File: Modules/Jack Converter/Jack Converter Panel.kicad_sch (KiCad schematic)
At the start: 39 parts

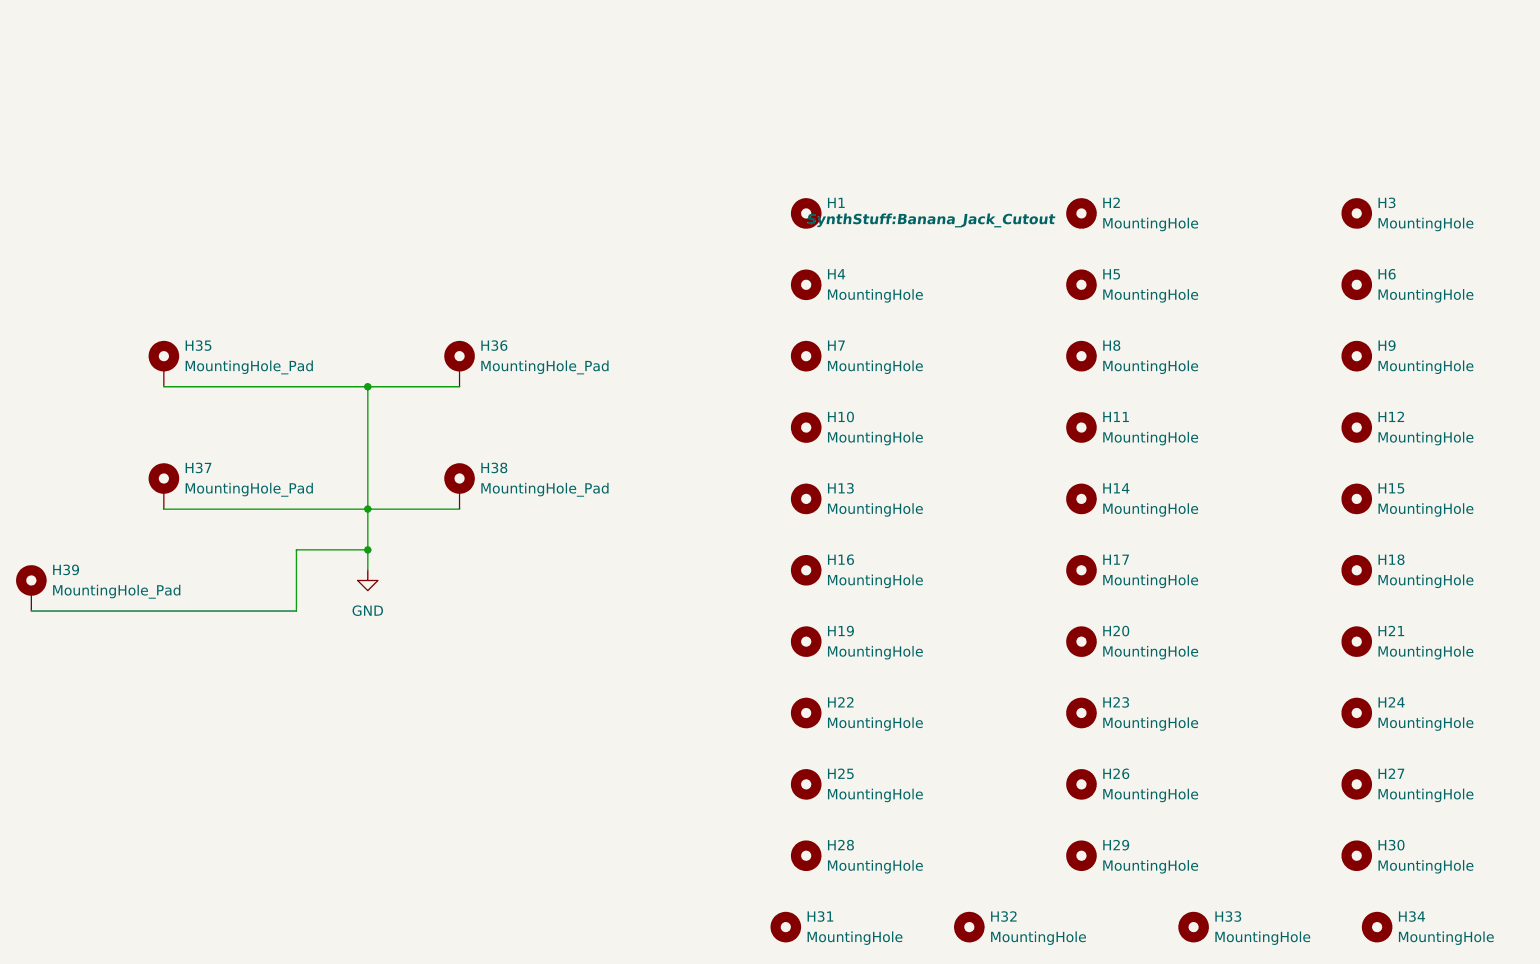
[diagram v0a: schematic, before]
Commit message: Front panel design ongoing
Deleted spacer hole, positioned all holes, started decals
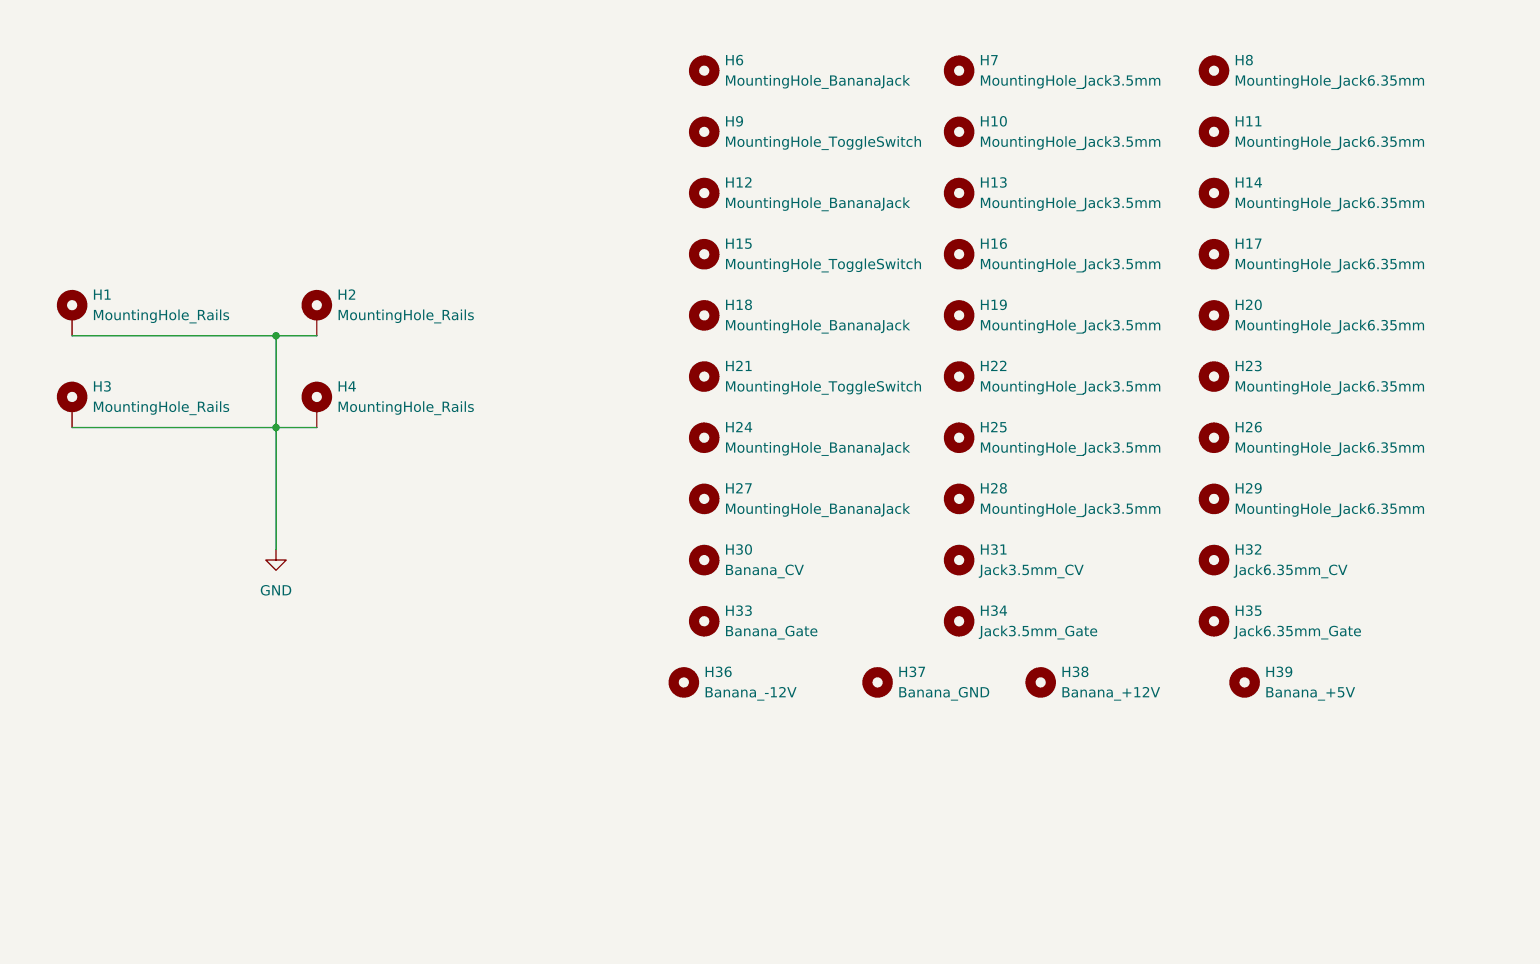
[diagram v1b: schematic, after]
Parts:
- removed H1: MountingHole, SynthStuff:Banana_Jack_Cutout, symbol Mechanical:MountingHole
- removed H10, H11, H12, H13, H14, H15, H16, H17, H18, H19, H2, H20, H21, H22, H23, H24, H25, H26, H27, H28, H29, H3, H30, H31, H32, H33, H34, H5, H6, H7, H8, H9: MountingHole, symbol Mechanical:MountingHole
- removed H35, H36, H37, H38, H39: MountingHole_Pad, SynthStuff:MountingHole_3.2mm_M3_Pad4mm, symbol Mechanical:MountingHole_Pad
- removed H4: MountingHole, SynthStuff:Toggle_Switch_Cutout, symbol Mechanical:MountingHole
- added H1, H2, H3, H4: MountingHole_Rails, SynthStuff:MountingHole_3.2mm_M3_Pad4mm, symbol Synth_Stuff:MountingHole_Rails
- added H10, H13, H16, H19, H22, H25, H28, H7: MountingHole_Jack3.5mm, SynthStuff:Jack_3.5mm_Cutout, symbol Synth_Stuff:MountingHole_Jack3.5mm
- added H11, H14, H17, H20, H23, H26, H29, H8: MountingHole_Jack6.35mm, SynthStuff:Jack_6.35mm_Cutout, symbol Synth_Stuff:MountingHole_Jack6.35mm
- added H12, H18, H24, H27, H6: MountingHole_BananaJack, SynthStuff:Banana_Jack_Cutout, symbol Synth_Stuff:MountingHole_BananaJack
- added H15, H21, H9: MountingHole_ToggleSwitch, SynthStuff:Toggle_Switch_Cutout, symbol Synth_Stuff:MountingHole_ToggleSwitch
- added H30: Banana_CV, SynthStuff:Banana_Jack_Cutout, symbol Synth_Stuff:MountingHole_BananaJack
- added H31: Jack3.5mm_CV, SynthStuff:Jack_3.5mm_Cutout, symbol Synth_Stuff:MountingHole_Jack3.5mm
- added H32: Jack6.35mm_CV, SynthStuff:Jack_6.35mm_Cutout, symbol Synth_Stuff:MountingHole_Jack6.35mm
- added H33: Banana_Gate, SynthStuff:Banana_Jack_Cutout, symbol Synth_Stuff:MountingHole_BananaJack
- added H34: Jack3.5mm_Gate, SynthStuff:Jack_3.5mm_Cutout, symbol Synth_Stuff:MountingHole_Jack3.5mm
- added H35: Jack6.35mm_Gate, SynthStuff:Jack_6.35mm_Cutout, symbol Synth_Stuff:MountingHole_Jack6.35mm
- added H36: Banana_-12V, SynthStuff:Banana_Jack_Cutout, symbol Synth_Stuff:MountingHole_BananaJack
- added H37: Banana_GND, SynthStuff:Banana_Jack_Cutout, symbol Synth_Stuff:MountingHole_BananaJack
- added H38: Banana_+12V, SynthStuff:Banana_Jack_Cutout, symbol Synth_Stuff:MountingHole_BananaJack
- added H39: Banana_+5V, SynthStuff:Banana_Jack_Cutout, symbol Synth_Stuff:MountingHole_BananaJack
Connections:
- net GND: now also H1.1, H2.1, H3.1, H4.1

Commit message: Finished
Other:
- company: (none) -> DMH
- title: (none) -> Adapter Mult Mk1
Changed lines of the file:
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@@
 	(generator_version "8.0")
 	(paper "A4")
+	(title_block
+		(title "Adapter Mult Mk1")
+		(date "2024-05-26")
+		(rev "1")
+		(company "DMH")
+	)
 	(junction
 		(at 109.22 64.77)

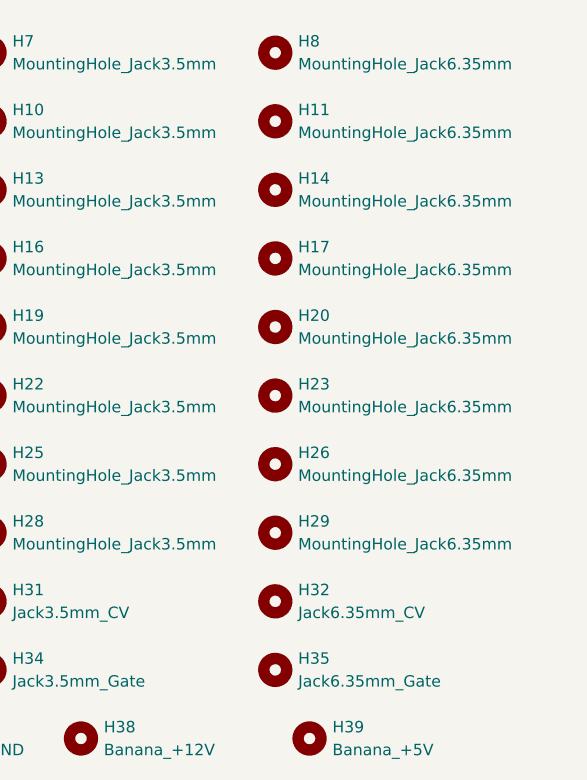
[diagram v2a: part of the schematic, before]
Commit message: Repositioned components on PCB
... in order to match front panel
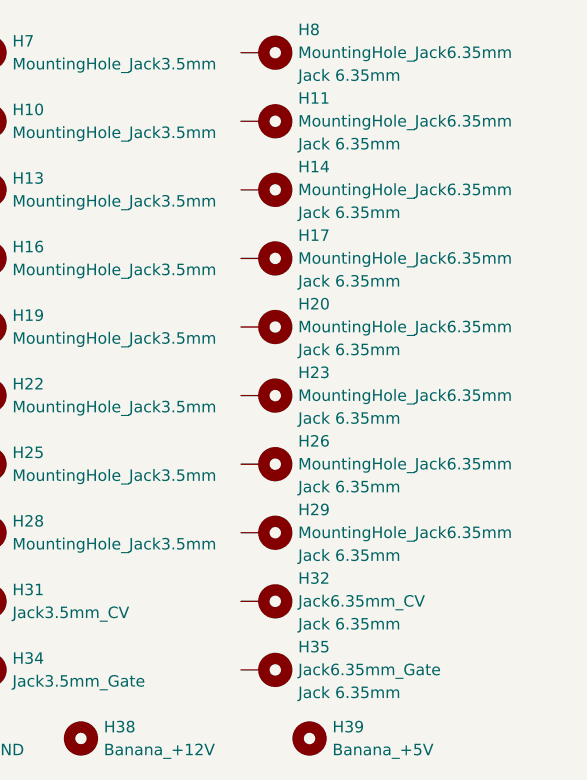
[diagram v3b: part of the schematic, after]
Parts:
- H11, H14, H17, H20, H23, H26, H29, H32, H35, H8: footprint SynthStuff:Jack_6.35mm_Cutout -> SynthStuff:Jack_6.35mm_Cutout_v2; symbol Synth_Stuff:MountingHole_Jack6.35mm -> Synth_Stuff:MountingHole_Jack6.35mm_v2

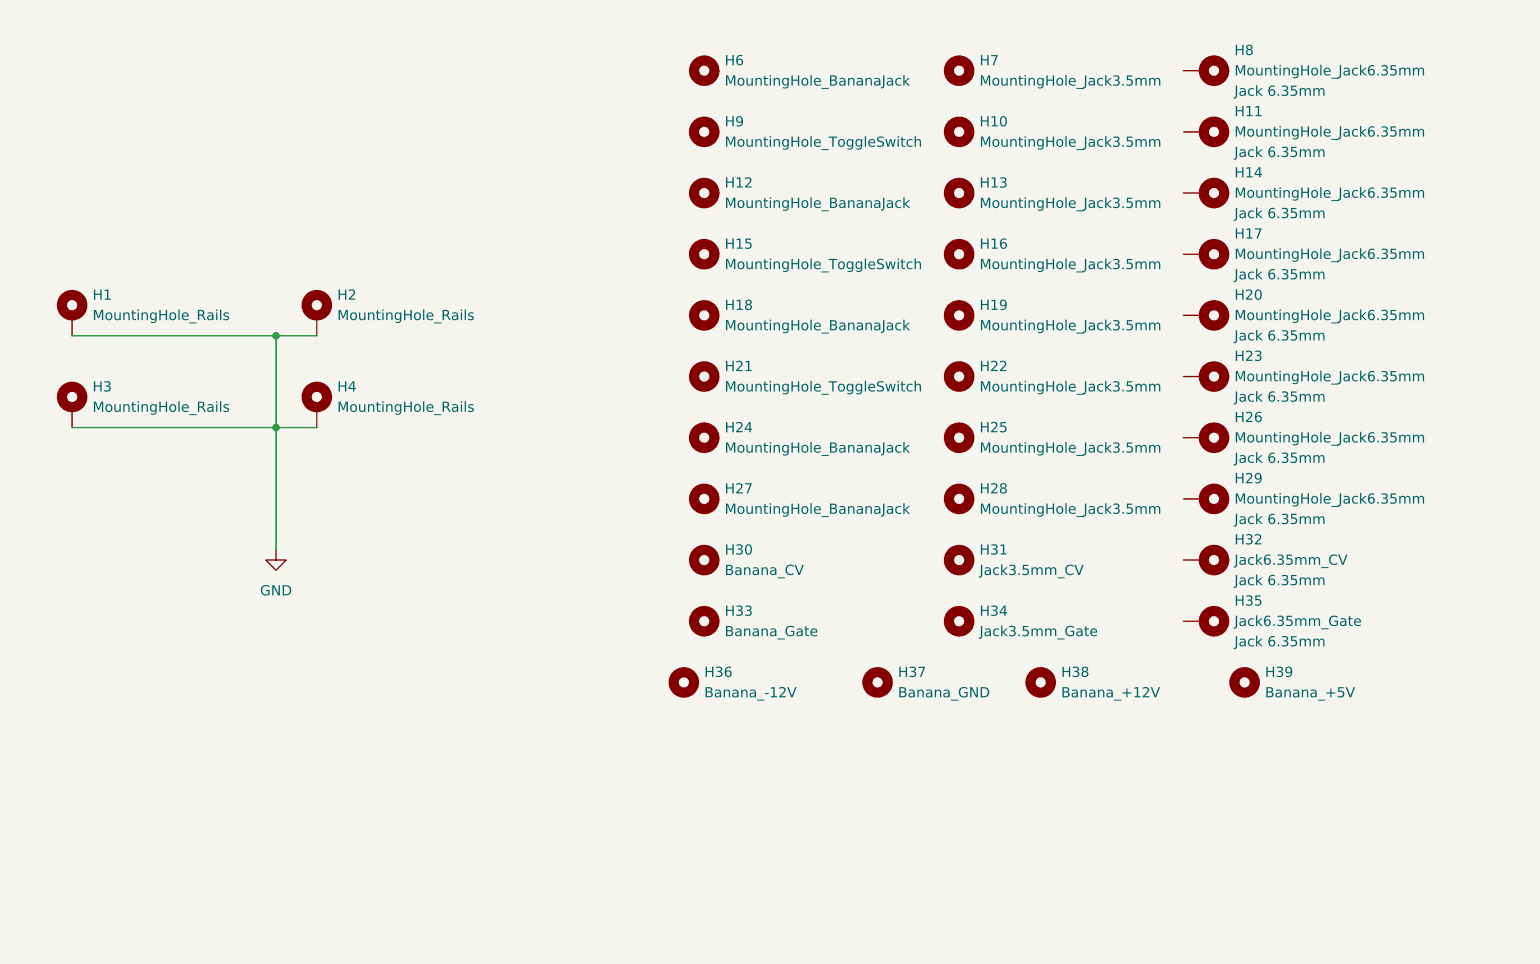
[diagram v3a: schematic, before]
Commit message: Replaced holes with the latest fp version
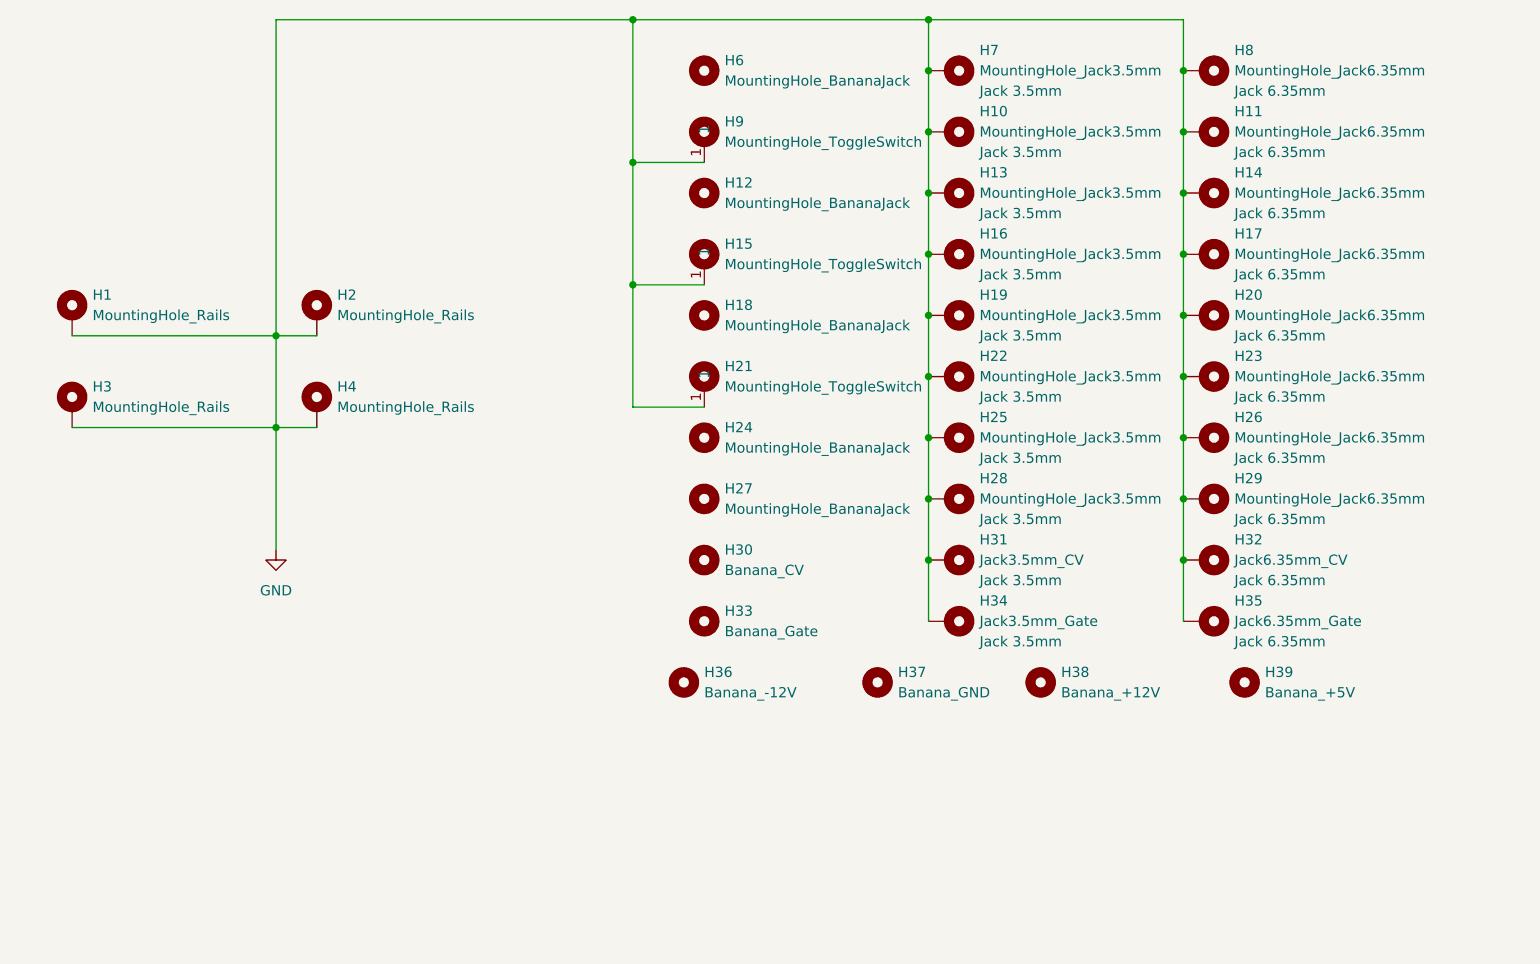
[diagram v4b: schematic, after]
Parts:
- H10, H13, H16, H19, H22, H25, H28, H31, H34, H7: footprint SynthStuff:Jack_3.5mm_Cutout -> SynthStuff:Jack_3.5mm_Cutout_v2; symbol Synth_Stuff:MountingHole_Jack3.5mm -> Synth_Stuff:MountingHole_Jack3.5mm_v2
- H12, H18, H24, H27, H30, H33, H36, H37, H38, H39, H6: footprint SynthStuff:Banana_Jack_Cutout -> SynthStuff:Banana_Jack_Cutout_v2
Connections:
- net GND: now also H10.1, H11.1, H13.1, H14.1, H15.1, H16.1, H17.1, H19.1, H20.1, H21.1, H22.1, H23.1, H25.1, H26.1, H28.1, H29.1, H31.1, H32.1, H34.1, H35.1, H7.1, H8.1, H9.1

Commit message: Updated jack footprints to 12mm washer
... and added hash art to Adapter Mult CV and Gate jacks
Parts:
- H1, H2, H3, H4: footprint SynthStuff:MountingHole_3.2mm_M3_Pad4mm -> SynthStuff:MountingHole_Rails
- H11, H14, H17, H20, H23, H26, H29, H32, H35, H8: footprint SynthStuff:Jack_6.35mm_Cutout_v2 -> SynthStuff:Jack_6.35mm_Cutout_v3
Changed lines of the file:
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@@
 			)
 		)
-		(property "Footprint" "SynthStuff:Jack_6.35mm_Cutout_v2"
+		(property "Footprint" "SynthStuff:Jack_6.35mm_Cutout_v3"
 			(at 226.06 46.99 0)
 			(effects
@@
 			)
 		)
-		(property "Footprint" "SynthStuff:Jack_6.35mm_Cutout_v2"
+		(property "Footprint" "SynthStuff:Jack_6.35mm_Cutout_v3"
 			(at 226.06 77.47 0)
 			(effects
@@
 			)
 		)
-		(property "Footprint" "SynthStuff:Jack_6.35mm_Cutout_v2"
+		(property "Footprint" "SynthStuff:Jack_6.35mm_Cutout_v3"
 			(at 226.06 69.85 0)
 			(effects
@@
 			)
 		)
-		(property "Footprint" "SynthStuff:Jack_6.35mm_Cutout_v2"
+		(property "Footprint" "SynthStuff:Jack_6.35mm_Cutout_v3"
 			(at 226.06 85.09 0)
 			(effects
@@
 			)
 		)
-		(property "Footprint" "SynthStuff:Jack_6.35mm_Cutout_v2"
+		(property "Footprint" "SynthStuff:Jack_6.35mm_Cutout_v3"
 			(at 226.06 100.33 0)
 			(effects
@@
 			)
 		)
-		(property "Footprint" "SynthStuff:MountingHole_3.2mm_M3_Pad4mm"
+		(property "Footprint" "SynthStuff:MountingHole_Rails"
 			(at 114.3 73.66 0)
 			(effects
@@
 			)
 		)
-		(property "Footprint" "SynthStuff:MountingHole_3.2mm_M3_Pad4mm"
+		(property "Footprint" "SynthStuff:MountingHole_Rails"
 			(at 114.3 62.23 0)
 			(effects
@@
 			)
 		)
-		(property "Footprint" "SynthStuff:Jack_6.35mm_Cutout_v2"
+		(property "Footprint" "SynthStuff:Jack_6.35mm_Cutout_v3"
 			(at 226.06 31.75 0)
 			(effects
@@
 			)
 		)
-		(property "Footprint" "SynthStuff:Jack_6.35mm_Cutout_v2"
+		(property "Footprint" "SynthStuff:Jack_6.35mm_Cutout_v3"
 			(at 226.06 39.37 0)
 			(effects
@@
 			)
 		)
-		(property "Footprint" "SynthStuff:Jack_6.35mm_Cutout_v2"
+		(property "Footprint" "SynthStuff:Jack_6.35mm_Cutout_v3"
 			(at 226.06 62.23 0)
 			(effects
@@
 			)
 		)
-		(property "Footprint" "SynthStuff:Jack_6.35mm_Cutout_v2"
+		(property "Footprint" "SynthStuff:Jack_6.35mm_Cutout_v3"
 			(at 226.06 54.61 0)
 			(effects
@@
 			)
 		)
-		(property "Footprint" "SynthStuff:Jack_6.35mm_Cutout_v2"
+		(property "Footprint" "SynthStuff:Jack_6.35mm_Cutout_v3"
 			(at 226.06 92.71 0)
 			(effects
@@
 			)
 		)
-		(property "Footprint" "SynthStuff:MountingHole_3.2mm_M3_Pad4mm"
+		(property "Footprint" "SynthStuff:MountingHole_Rails"
 			(at 83.82 73.66 0)
 			(effects
@@
 			)
 		)
-		(property "Footprint" "SynthStuff:MountingHole_3.2mm_M3_Pad4mm"
+		(property "Footprint" "SynthStuff:MountingHole_Rails"
 			(at 83.82 62.23 0)
 			(effects
